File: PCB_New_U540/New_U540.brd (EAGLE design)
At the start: 118 x 207 mm, 82 parts, among them IC1 TXB0108PWR, IC2 TXB0108PWR, IC3 TPS76201DBVR, IC4 TPS76201DBVR, IC5 TPS76201DBVR, J4 2985-6004, J5 2985-6004, Q1 BSH103,235, Q2 BSH103,235, Q3 BSH103,235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

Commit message: Change regulators for higher current
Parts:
- removed R1, R4, R7: 113k, SparkFun-Resistors:1206
- removed R2, R5, R8: 66.5k, SparkFun-Resistors:1206
- removed R3, R6, R9: 1, SparkFun-Resistors:1206
- C10, C8: value 4.7uF -> 22uF
- C5: value 4.7uF -> 100uF
- C6: value 1.0uF -> 22uF
- C7, C9: value 1.0uF -> 100uF
- IC3, IC4, IC5: value TPS76201DBVR -> AMS1117-1.8; device SamacSys_Parts:SOT95P280X145-5N -> SamacSys_Parts:SOT229P700X180-4N
- moved C10 31.6 mm to (-50.0, 97.5), turned to 90 degrees
- moved IC5 26.5 mm to (-44.0, 98.0)
- moved C9 26.3 mm to (-37.5, 97.5), turned to 270 degrees
- moved C6 19.7 mm to (-50.5, 84.0)
- moved C7 19.3 mm to (-38.0, 68.0), turned to 270 degrees
- moved IC4 19.1 mm to (-44.0, 68.0)
- moved IC3 18.1 mm to (-44.0, 83.5)
- moved C5 15.4 mm to (-38.0, 83.5)
- moved C8 13.8 mm to (-50.0, 68.0), turned to 90 degrees
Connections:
- removed net N$16: IC3.4, R1.1, R2.2
- removed net N$17: C5.2, R3.2
- removed net N$18: IC4.4, R4.1, R5.2
- removed net N$19: C8.2, R6.2
- removed net N$20: IC5.4, R7.1, R8.2
- removed net N$21: C10.2, R9.2
- net GND: now also C10.2, C5.2, C8.2, IC3.1, IC4.1, IC5.1; no longer IC3.2, IC3.3, IC4.2, IC4.3, IC5.2, IC5.3, R2.1, R3.1, R5.1, R6.1, R8.1, R9.1
- net VDD_1.8_1: now also C10.1, IC5.2, IC5.4; no longer C5.1, IC3.5, R1.2
- net VDD_1.8_2: now also C6.1, IC3.2, IC3.4; no longer C8.1, IC4.5, R4.2
- net VDD_1.8_3: now also C8.1, IC4.2, IC4.4; no longer C10.1, IC5.5, R7.2
- net VDD_3V3: now also C5.1, IC3.3, IC4.3, IC5.3; no longer C6.1, IC3.1, IC4.1, IC5.1
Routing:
- net GND: track 982.5 -> 914.4 mm, vias 322 -> 357
- net VDD_3V3: track 479.5 -> 471.9 mm
- net N$18: track 5.55 -> 0.00 mm
- net N$16: track 5.55 -> 0.00 mm
- net N$20: track 5.55 -> 0.00 mm
- net VDD_1.8_2: track 136.1 -> 140.9 mm
- net N$21: track 3.50 -> 0.00 mm
- net N$19: track 3.50 -> 0.00 mm
- net N$17: track 3.50 -> 0.00 mm
- net VDD_1.8_3: track 116.3 -> 119.6 mm
- net VDD_1.8_1: track 154.6 -> 156.7 mm
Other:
- board text added: "127"
- board text added: "128"
- board text added: "129"
- board text added: "130"
- board text added: "191"
- board text added: "192"
- board text added: "193"
- board text added: "194"
- board text added: "255"
- board text added: "256"
- board text added: "63"
- board text added: "64"
- board text added: "65"
- board text added: "66"

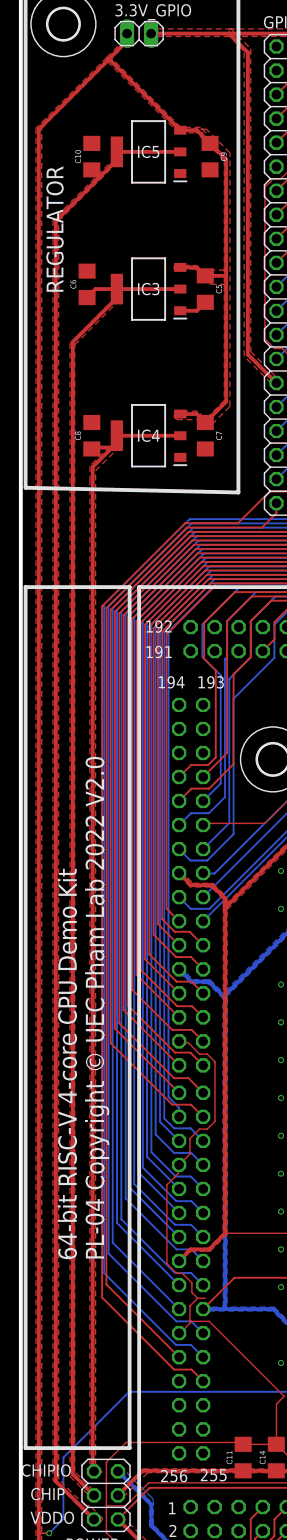
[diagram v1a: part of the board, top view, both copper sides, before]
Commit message: Update boom file
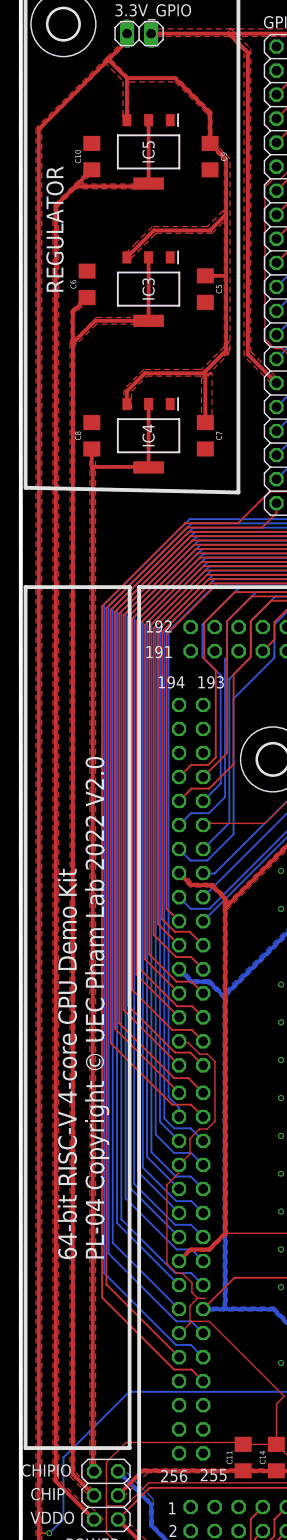
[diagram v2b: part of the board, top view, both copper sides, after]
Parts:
- turned IC3 to 270 degrees
- turned IC4 to 270 degrees
- turned IC5 to 270 degrees
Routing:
- net VDD_3V3: track 471.9 -> 495.1 mm
- net VDD_1.8_1: track 156.7 -> 160.5 mm
- net GND: track 914.4 -> 911.4 mm
- net VDD_1.8_2: track 140.9 -> 143.8 mm
- net VDD_1.8_3: track 119.6 -> 121.0 mm
